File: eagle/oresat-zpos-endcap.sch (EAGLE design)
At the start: 47 parts, among them J7 1.27MM-SWD-CONNECTOR, U1 TPS63070, U2 TCAN330, U6 STM32F042K6, X1 16MHZ-2.5x2mm

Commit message: Not done, but checking in anyway. Lots left to do, trying to figure out where things go.
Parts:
- removed J5: (no value), SparkFun-Connectors:6_PIN_SERIAL_TARGETSILK
- removed JP3: (no value), pinhead:PINHD-1X3
- removed JP4: (no value), pinhead:PINHD-2X10
- removed JP5, JP6, JP7: (no value), pinhead:PINHD-1X5
- removed JP8: (no value), pinhead:PINHD-1X2
- added C1, C10, C2, C7: 100n, rcl_custom:C-EU0402-B-NOSILK
- added C12, C13: 10u, oresat-rcl:C-EU0603-B-NOSILK
- added C15, C19: 4.7u, oresat-rcl:C-EU0603-B-NOSILK
- added R4, R5: 4.7k, rcl_custom:R-US_0402-B-NOSILK
- added U3, U4: HMC5883L, monitor-v2:HMC5883L-LGA-16
- CF1: value ORESAT-SOLARPANEL-12PIN -> J-HARWIN-M55-6021242R; device oresat-connectors:ORESAT-SOLARPANEL-12PIN -> J-Harwin-M55-6021242R:J-HARWIN-M55-6021242R
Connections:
- removed net N$406: J5.VCC, JP8.2
- new net N$2: C12.1, U3.C1
- new net N$3: U4.DRDY
- new net N$4: U3.DRDY
- new net N$5: C13.1, U4.C1
- net 3.3V: now also C1.2, C10.2, C15.1, C19.1, C2.2, C7.2, R4.2, R5.2, U3.VDD, U3.VDD_IO, U4.VDD, U4.VDD_IO; no longer JP5.1, JP5.2, JP5.3, JP5.4, JP5.5, JP6.1, JP6.2, JP6.3, JP6.4, JP6.5
- net GND: now also C1.1, C10.1, C12.2, C13.2, C15.2, C19.2, C2.1, C7.1, CF1.SHIELDS, U3.GND11, U3.GND9, U4.GND11, U4.GND9; no longer J5.GND, JP4.15, JP4.17, JP4.19
- net PA0: no longer JP4.2
- net PA1: no longer JP4.4
- net PA15: no longer JP4.11
- net PA2/USART2_TX: no longer J5.TXO, JP4.6
- net PA3/USART2_RX: no longer J5.RXI, JP4.8
- net PA4: no longer JP4.10
- net PA5/SPI1_SCK: no longer JP4.12
- net PA6/SPI1_MISO: no longer JP4.14
- net PA7/SPI1_MOSI: no longer JP4.16
- net PA8: no longer JP4.13
- net PB0: no longer JP4.18
- net PB1: no longer JP4.20
- net PB3: no longer JP4.9
- net PB4: no longer JP4.7
- net PB5: no longer JP4.5
- net PB6/SCL: now also R4.1, U3.SCL, U4.SCL; no longer JP4.3
- net PB7/SDA: now also R5.1, U3.SDA, U4.SDA; no longer JP4.1
- net VBUS: no longer JP3.1, JP3.2, JP3.3, JP7.1, JP7.2, JP7.3, JP7.4, JP7.5, JP8.1
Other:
- note added: "+X+Y Corner"
- note added: "-X-Y Corner"
- note added: "OreSat +Z End Card"
- note removed: "Meant for FTDI TTL-232R-3V3 cable"
- note removed: "OreSat Proto-Card"
- note removed: "Power VBUS from USB 5V (DEV ONLY)"
- moved on the sheet: C11, C14, C16, C17, C18, C22, C25, C3, C4, C5, C6, C8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

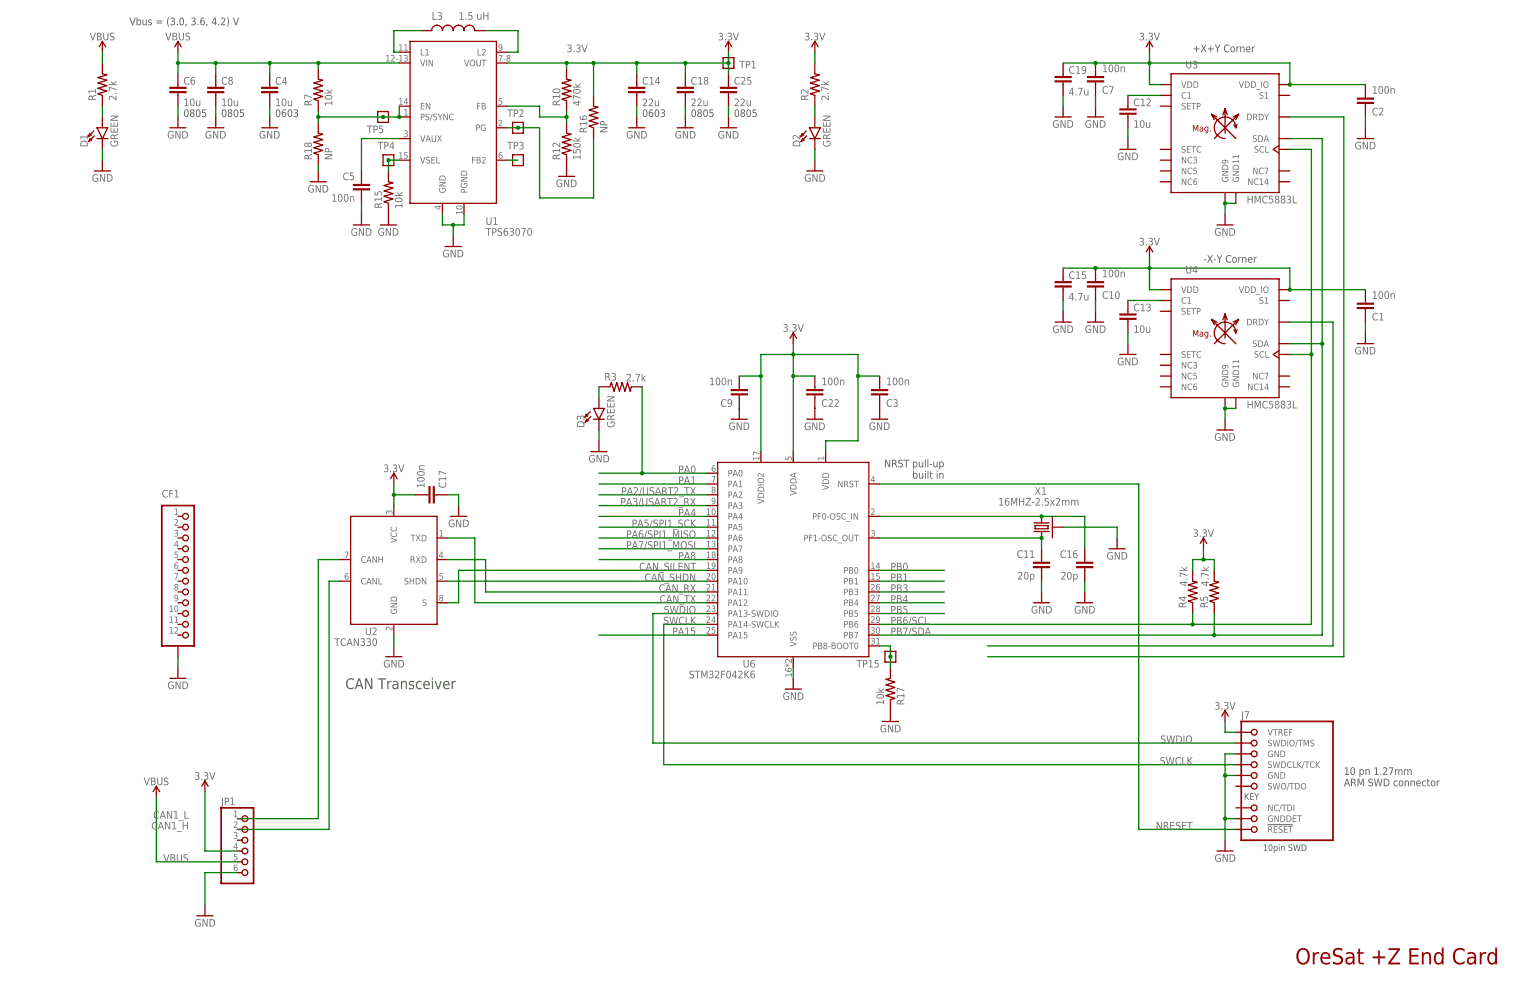
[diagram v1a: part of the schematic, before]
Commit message: Removed SPS + uC blocks; only magnetometers remain on the end cap. Not great for future expandability, but moves uC to the end card where it's more useful.
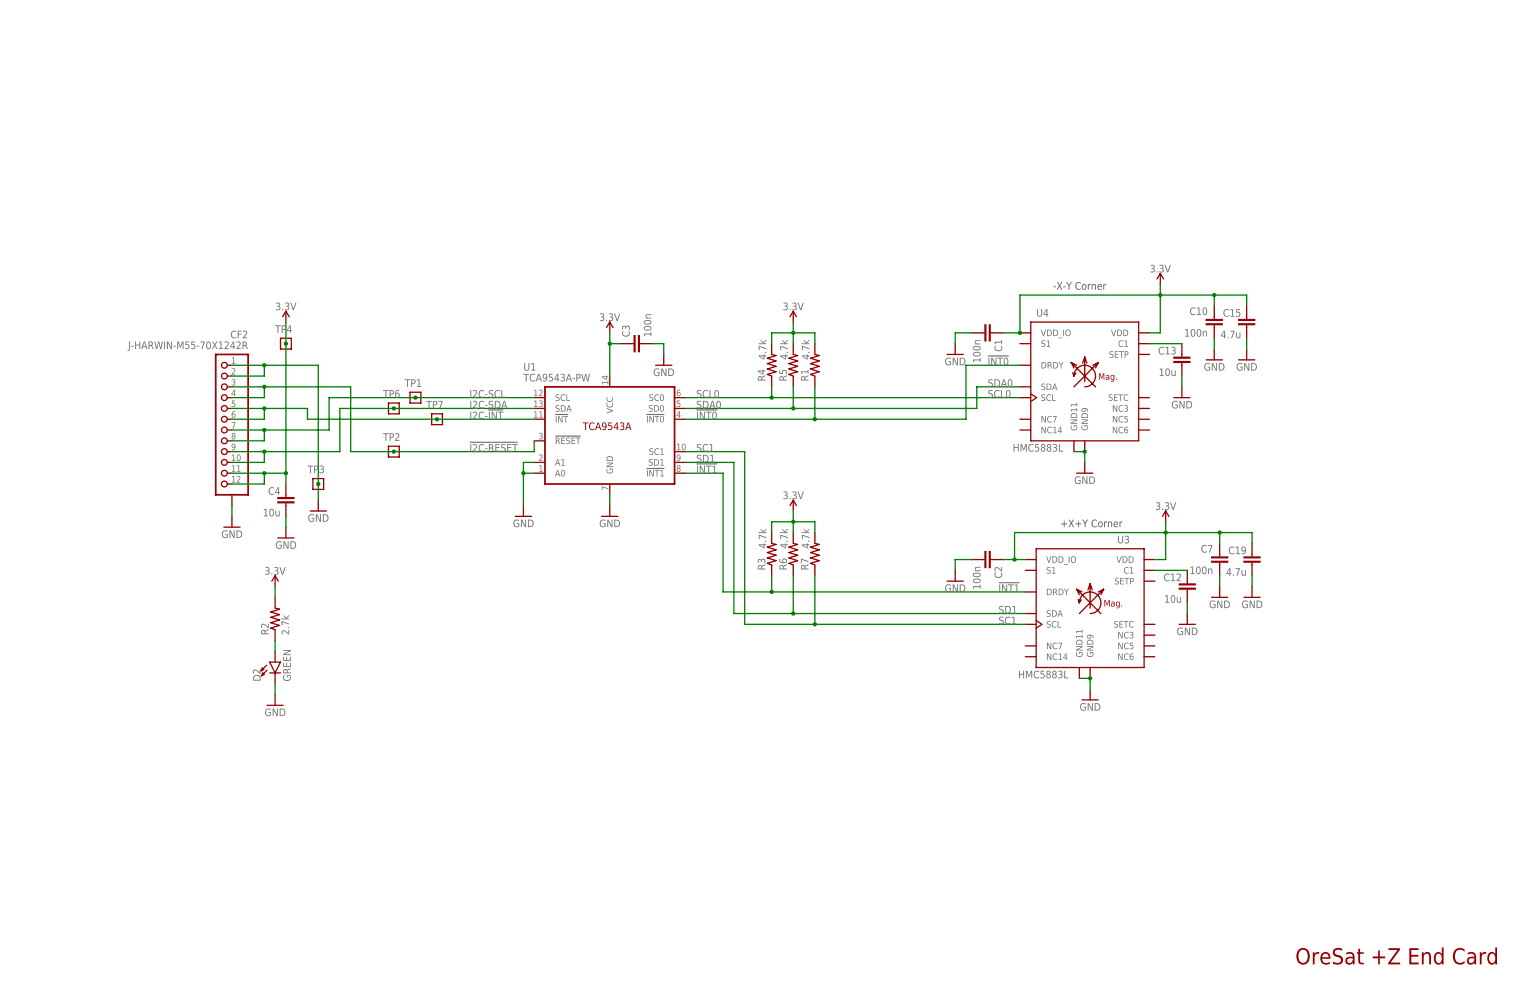
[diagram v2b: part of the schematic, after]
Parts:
- removed C11, C16: 20p, rcl_custom:C-EU0402-B-NOSILK
- removed C14: 22u, oresat-rcl:C-EU0603-B-NOSILK
- removed C17, C22, C5, C9: 100n, rcl_custom:C-EU0402-B-NOSILK
- removed C18, C25: 22u, oresat-rcl:C-EU0805-B-NOSILK
- removed C6, C8: 10u, oresat-rcl:C-EU0805-B-NOSILK
- removed CF1: J-HARWIN-M55-6021242R, J-Harwin-M55-6021242R:J-HARWIN-M55-6021242R
- removed D1, D3: GREEN, SparkFun-LED:LED-GREEN0603
- removed J7: 1.27MM-SWD-CONNECTOR, J-CNC-3220-10-0100-00-ARM-SWD-port:1.27MM-SWD-CONNECTOR
- removed JP1: (no value), pinhead:PINHD-1X6
- removed L3: 1.5 uH, L-Coilcraft-XFL4020:L-COILCRAFT-XFL4020
- removed R10: 470k, rcl_custom:R-US_0402-B-NOSILK
- removed R12: 150k, rcl_custom:R-US_0402-B-NOSILK
- removed R15, R17: 10k, rcl_custom:R-US_0402-B-NOSILK
- removed R16, R18: NP, rcl_custom:R-US_0402-B-NOSILK
- removed TP15, TP5: TEST-POINT, Tova:TEST-POINT
- removed U2: TCAN330, TCAN330:TCAN330
- removed U6: STM32F042K6, STM32F042K:STM32F042K6
- removed X1: 16MHZ-2.5x2mm, low-gain-radio:CRYSTAL-WITH-GND
- added CF2: J-HARWIN-M55-70X1242R, J-Harwin-M55-70X1242R-12pin-1.27mm-M-vertical:J-HARWIN-M55-70X1242R
- added R6: 4.7k, rcl_custom:R-US_0402-B-NOSILK
- added TP6, TP7: TEST-POINT, Tova:TEST-POINT
- R1, R3: value 2.7k -> 4.7k
- R7: value 10k -> 4.7k
- U1: value TPS63070 -> TCA9543A-PW; device ic-pwr-tps63070x:TPS63070X -> U-TI-TCA9543A-I2C-2-to-1-multiplexer:TCA9543A-PW; DIS Digi-Key -> (none); DPN 296-44874-1-ND -> (none); MFR TI -> (none); MPN TPS63070 -> (none)
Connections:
- removed net BOOT: R17.2, TP15.1, U6.PB8-BOOT0
- removed net CAN1_H: JP1.1, U2.CANH
- removed net CAN1_L: JP1.2, U2.CANL
- removed net CAN_RX: U2.RXD, U6.PA11
- removed net CAN_SHDN: U2.SHDN, U6.PA10
- removed net CAN_SILENT: U2.S, U6.PA9
- removed net CAN_TX: U2.TXD, U6.PA12
- removed net CRYSTALIN: C16.1, U6.PF0-OSC_IN, X1.1
- removed net CRYSTALOUT: C11.1, U6.PF1-OSC_OUT, X1.2
- removed net N$1: D3.A, R3.1
- removed net N$270: D1.A, R1.1
- removed net N$3: U4.DRDY
- removed net N$4: U3.DRDY
- removed net NRESET: J7.!RESET, U6.NRST
- removed net PA0: R3.2, U6.PA0
- removed net PA1: U6.PA1
- removed net PA15: U6.PA15
- removed net PA2/USART2_TX: U6.PA2
- removed net PA3/USART2_RX: U6.PA3
- removed net PA4: U6.PA4
- removed net PA5/SPI1_SCK: U6.PA5
- removed net PA6/SPI1_MISO: U6.PA6
- removed net PA7/SPI1_MOSI: U6.PA7
- removed net PA8: U6.PA8
- removed net PB0: U6.PB0
- removed net PB1: U6.PB1
- removed net PB3: U6.PB3
- removed net PB4: U6.PB4
- removed net PB5: U6.PB5
- removed net PB6/SCL: R4.1, U3.SCL, U4.SCL, U6.PB6
- removed net PB7/SDA: R5.1, U3.SDA, U4.SDA, U6.PB7
- removed net SWCLK: J7.SWDCLK/TCK, U6.PA14-SWCLK
- removed net SWDIO: J7.SWDIO/TMS, U6.PA13-SWDIO
- removed net TPS-EN1: R18.2, R7.1, TP5.1, U1.EN, U1.PS/SYNC
- removed net TPS-FB1: R10.1, R12.2, U1.FB
- removed net TPS-FB3: TP3.1, U1.FB2
- removed net TPS-L3: L3.1, U1.L1
- removed net TPS-L4: L3.2, U1.L2
- removed net TPS-PG1: R16.1, TP2.1, U1.PG
- removed net TPS-VAUX1: C5.1, U1.VAUX
- removed net TPS-VSEL1: R15.2, TP4.1, U1.VSEL
- removed net VBUS: C4.1, C6.1, C8.1, JP1.5, R1.2, R7.2, U1.VIN
- new net !I2C-RESET: CF2.3, CF2.4, TP2.1, U1.!RESET
- new net !INT0: R1.1, U1.!INT0, U4.DRDY
- new net !INT1: R3.1, U1.!INT1, U3.DRDY
- new net I2C-!INT: CF2.5, CF2.6, TP7.1, U1.!INT
- new net I2C-SCL: CF2.7, CF2.8, TP1.1, U1.SCL
- new net I2C-SDA: CF2.10, CF2.9, TP6.1, U1.SDA
- new net SC1: R7.1, U1.SC1, U3.SCL
- new net SCL0: R4.1, U1.SC0, U4.SCL
- new net SD1: R6.1, U1.SD1, U3.SDA
- new net SDA0: R5.1, U1.SD0, U4.SDA
- net 3.3V: now also C1.1, C10.1, C2.1, C3.1, C4.1, C7.1, CF2.11, CF2.12, R1.2, R3.2, R6.2, R7.2, TP4.1, U1.VCC; no longer C1.2, C10.2, C14.1, C17.2, C18.1, C2.2, C22.2, C25.1, C3.2, C7.2, C9.2, J7.VTREF, JP1.4, R10.2, R16.2, TP1.1, U1.VOUT, U2.VCC, U6.VDD, U6.VDDA, U6.VDDIO2
- net GND: now also C1.2, C10.2, C2.2, C3.2, C7.2, CF2.1, CF2.2, CF2.SHIELDS, TP3.1, U1.A0, U1.A1; no longer C1.1, C10.1, C11.2, C14.2, C16.2, C17.1, C18.2, C2.1, C22.1, C25.2, C3.1, C5.2, C6.2, C7.1, C8.2, C9.1, CF1.SHIELDS, D1.C, D3.C, J7.GND, J7.GND@2, J7.GNDDET, JP1.6, R12.1, R15.1, R17.1, R18.1, U1.PGND, U2.GND, U6.VSS, X1.SHIELD
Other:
- note removed: "0603"
- note removed: "0805"
- note removed: "10 pn 1.27mm ARM SWD connector"
- note removed: "CAN Transceiver"
- note removed: "NRST pull-up built in"
- note removed: "Vbus = (3.0, 3.6, 4.2) V"
- moved on the sheet: C1, C10, C12, C13, C15, C19, C2, C3, C4, C7, D2, R1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
